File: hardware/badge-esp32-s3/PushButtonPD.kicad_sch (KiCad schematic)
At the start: 3 parts, among them SW1 TS665CJ

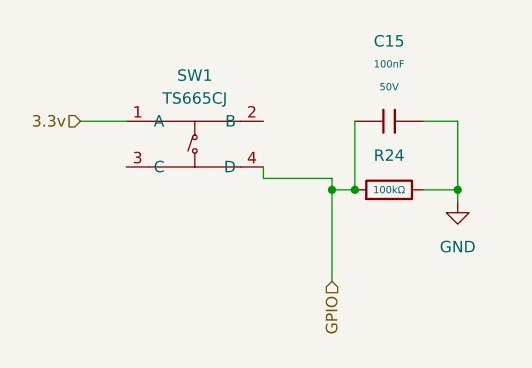
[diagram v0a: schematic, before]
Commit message: Resistor Fix
PD resistor 100k -> 47k
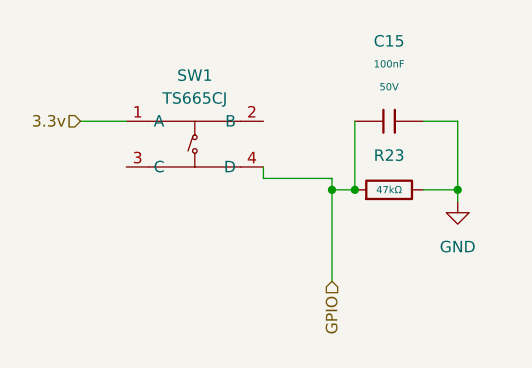
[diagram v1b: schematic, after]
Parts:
- removed R24: 100kΩ, PCM_JLCPCB:R_0805, symbol PCM_JLCPCB-Resistors:0805,100kΩ
- added R23: 47kΩ, PCM_JLCPCB:R_0805, symbol PCM_JLCPCB-Resistors:0805,47kΩ
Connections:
- net GND: now also R23.2
- net GPIO: now also R23.1

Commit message: Reapply "Merge branch 'main' into Danny"
This reverts commit 522ccfdb580e54901b8ff562dc2e90cfc327c6b7.
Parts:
- removed C15: 100nF, PCM_JLCPCB:C_0805, symbol PCM_JLCPCB-Capacitors:0805,100nF,(2)
- removed R23: 47kΩ, PCM_JLCPCB:R_0805, symbol PCM_JLCPCB-Resistors:0805,47kΩ
- added C15: 1uF, PCM_JLCPCB:C_0603, symbol PCM_JLCPCB-Capacitors:0603,1uF
- added R23, R31: 10kΩ, PCM_JLCPCB:R_0603, symbol PCM_JLCPCB-Resistors:0603,10kΩ
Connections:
- net GND: now also C15.2, R31.2
- net GPIO: now also C15.1, R23.2, R31.1; no longer SW1.4 (D)
- new net: R23.1, SW1.4 (D)

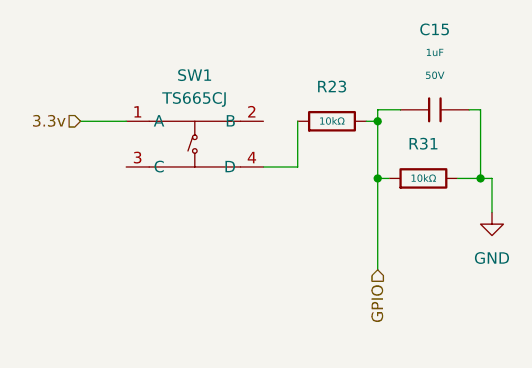
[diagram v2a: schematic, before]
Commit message: Revert "Merge branch 'main' into Danny"
This reverts commit f39a0d75d6025751b3d0be32cc251741b689ee9f, reversing
changes made to 38c8f4414de6e086c66d277d9ce522e64904a3dc.
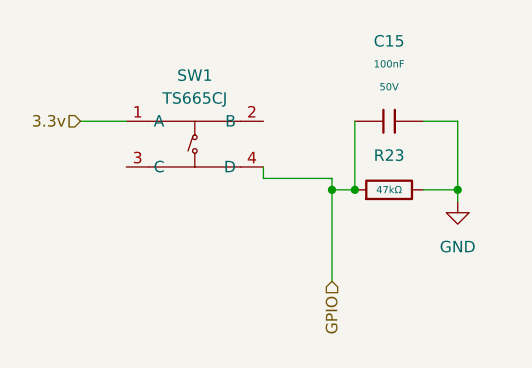
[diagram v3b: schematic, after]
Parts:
- removed C15: 1uF, PCM_JLCPCB:C_0603, symbol PCM_JLCPCB-Capacitors:0603,1uF
- removed R23, R31: 10kΩ, PCM_JLCPCB:R_0603, symbol PCM_JLCPCB-Resistors:0603,10kΩ
- added C15: 100nF, PCM_JLCPCB:C_0805, symbol PCM_JLCPCB-Capacitors:0805,100nF,(2)
- added R23: 47kΩ, PCM_JLCPCB:R_0805, symbol PCM_JLCPCB-Resistors:0805,47kΩ
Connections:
- net GND: now also C15.2, R23.2
- net GPIO: now also SW1.4 (D), C15.1, R23.1

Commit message: Updated PD schematic
Changed the button debounce schematic.
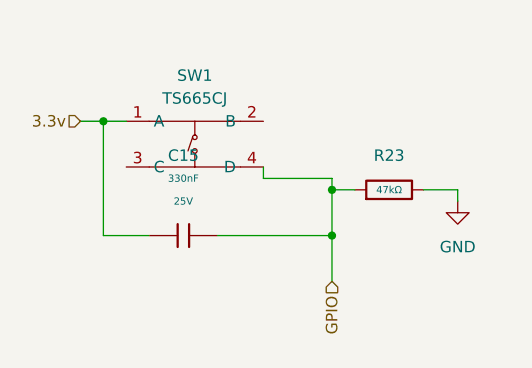
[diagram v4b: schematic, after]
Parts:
- removed C15: 100nF, PCM_JLCPCB:C_0805, symbol PCM_JLCPCB-Capacitors:0805,100nF,(2)
- added C15: 330nF, PCM_JLCPCB:C_0603, symbol PCM_JLCPCB-Capacitors:0603,330nF
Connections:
- net 3.3v: now also C15.1
- net GPIO: now also C15.2
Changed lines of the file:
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@@
 	)
 	(junction
-		(at 138.43 76.2)
+		(at 135.89 81.28)
 		(diameter 0)
 		(color 0 0 0 0)
 	)
 	(junction
-		(at 149.86 76.2)
+		(at 110.49 68.58)
 		(diameter 0)
 		(color 0 0 0 0)
@@
 	(wire
 		(pts
-			(xy 149.86 68.58) (xy 149.86 76.2)
-		)
-		(stroke
-			(width 0)
-			(type default)
-		)
-	)
-	(wire
-		(pts
 			(xy 135.89 74.93) (xy 135.89 76.2)
 		)
@@
 	(wire
 		(pts
-			(xy 146.05 68.58) (xy 149.86 68.58)
-		)
-		(stroke
-			(width 0)
-			(type default)
-		)
-	)
-	(wire
-		(pts
-			(xy 107.95 68.58) (xy 113.03 68.58)
+			(xy 107.95 68.58) (xy 110.49 68.58)
 		)
 		(stroke
@@
 	(wire
 		(pts
+			(xy 135.89 81.28) (xy 135.89 86.36)
+		)
+		(stroke
+			(width 0)
+			(type default)
+		)
+	)
+	(wire
+		(pts
 			(xy 128.27 74.93) (xy 135.89 74.93)
 		)
@@
 	(wire
 		(pts
-			(xy 135.89 76.2) (xy 135.89 86.36)
-		)
-		(stroke
-			(width 0)
-			(type default)
-		)
-	)
-	(wire
-		(pts
-			(xy 138.43 68.58) (xy 138.43 76.2)
+			(xy 135.89 76.2) (xy 135.89 81.28)
+		)
+		(stroke
+			(width 0)
+			(type default)
+		)
+	)
+	(wire
+		(pts
+			(xy 123.19 81.28) (xy 135.89 81.28)
+		)
+		(stroke
+			(width 0)
+			(type default)
+		)
+	)
+	(wire
+		(pts
+			(xy 110.49 81.28) (xy 110.49 68.58)
+		)
+		(stroke
+			(width 0)
+			(type default)
+		)
+	)
+	(wire
+		(pts
+			(xy 115.57 81.28) (xy 110.49 81.28)
 		)
 		(stroke
@@
 		(pts
 			(xy 146.05 76.2) (xy 149.86 76.2)
+		)
+		(stroke
+			(width 0)
+			(type default)
+		)
+	)
+	(wire
+		(pts
+			(xy 110.49 68.58) (xy 113.03 68.58)
 		)
 		(stroke
@@
 	)
 	(symbol
-		(lib_id "PCM_JLCPCB-Capacitors:0805,100nF,(2)")
-		(at 142.24 68.58 90)
+		(lib_id "PCM_JLCPCB-Capacitors:0603,330nF")
+		(at 119.38 81.28 90)
 		(unit 1)
 		(exclude_from_sim no)
@@
 		(fields_autoplaced yes)
 		(property "Reference" "C15"
-			(at 142.24 59.69 90)
-			(effects
-				(font
-					(size 1.27 1.27)
-				)
-			)
-		)
-		(property "Value" "100nF"
-			(at 142.24 62.23 90)
+			(at 119.38 72.39 90)
+			(effects
+				(font
+					(size 1.27 1.27)
+				)
+			)
+		)
+		(property "Value" "330nF"
+			(at 119.38 74.93 90)
 			(effects
 				(font
@@
 			)
 		)
-		(property "Footprint" "PCM_JLCPCB:C_0805"
-			(at 142.24 70.358 90)
-			(effects
-				(font
-					(size 1.27 1.27)
-				)
-				(hide yes)
-			)
-		)
-		(property "Datasheet" "https://www.lcsc.com/datasheet/lcsc_datasheet_2304140030_YAGEO-CC0805KRX7R9BB104_C49678.pdf"
-			(at 142.24 68.58 0)
-			(effects
-				(font
-					(size 1.27 1.27)
-				)
-				(hide yes)
-			)
-		)
-		(property "Description" "50V 100nF X7R ±10% 0805 Multilayer Ceramic Capacitors MLCC - SMD/SMT ROHS"
-			(at 142.24 68.58 0)
-			(effects
-				(font
-					(size 1.27 1.27)
-				)
-				(hide yes)
-			)
-		)
-		(property "LCSC" "C49678"
-			(at 142.24 68.58 0)
-			(effects
-				(font
-					(size 1.27 1.27)
-				)
-				(hide yes)
-			)
-		)
-		(property "Stock" "23739199"
-			(at 142.24 68.58 0)
-			(effects
-				(font
-					(size 1.27 1.27)
-				)
-				(hide yes)
-			)
-		)
-		(property "Price" "0.008USD"
-			(at 142.24 68.58 0)
+		(property "Footprint" "PCM_JLCPCB:C_0603"
+			(at 119.38 83.058 90)
+			(effects
+				(font
+					(size 1.27 1.27)
+				)
+				(hide yes)
+			)
+		)
+		(property "Datasheet" "https://www.lcsc.com/datasheet/lcsc_datasheet_2304140030_FH--Guangdong-Fenghua-Advanced-Tech-0603B334K250NT_C1615.pdf"
+			(at 119.38 81.28 0)
+			(effects
+				(font
+					(size 1.27 1.27)
+				)
+				(hide yes)
+			)
+		)
+		(property "Description" "25V 330nF X7R ±10% 0603 Multilayer Ceramic Capacitors MLCC - SMD/SMT ROHS"
+			(at 119.38 81.28 0)
+			(effects
+				(font
+					(size 1.27 1.27)
+				)
+				(hide yes)
+			)
+		)
+		(property "LCSC" "C1615"
+			(at 119.38 81.28 0)
+			(effects
+				(font
+					(size 1.27 1.27)
+				)
+				(hide yes)
+			)
+		)
+		(property "Stock" "122277"
+			(at 119.38 81.28 0)
+			(effects
+				(font
+					(size 1.27 1.27)
+				)
+				(hide yes)
+			)
+		)
+		(property "Price" "0.014USD"
+			(at 119.38 81.28 0)
 			(effects
 				(font
@@
 		)
 		(property "Process" "SMT"
-			(at 142.24 68.58 0)
+			(at 119.38 81.28 0)
 			(effects
 				(font
@@
 		)
 		(property "Minimum Qty" "20"
-			(at 142.24 68.58 0)
+			(at 119.38 81.28 0)
 			(effects
 				(font
@@
 		)
 		(property "Attrition Qty" "10"
-			(at 142.24 68.58 0)
-			(effects
-				(font
-					(size 1.27 1.27)
-				)
-				(hide yes)
-			)
-		)
-		(property "Class" "Basic Component"
-			(at 142.24 68.58 0)
+			(at 119.38 81.28 0)
+			(effects
+				(font
+					(size 1.27 1.27)
+				)
+				(hide yes)
+			)
+		)
+		(property "Class" "Preferred Component"
+			(at 119.38 81.28 0)
 			(effects
 				(font
@@
 		)
 		(property "Category" "Capacitors,Multilayer Ceramic Capacitors MLCC - SMD/SMT"
-			(at 142.24 68.58 0)
-			(effects
-				(font
-					(size 1.27 1.27)
-				)
-				(hide yes)
-			)
-		)
-		(property "Manufacturer" "YAGEO"
-			(at 142.24 68.58 0)
-			(effects
-				(font
-					(size 1.27 1.27)
-				)
-				(hide yes)
-			)
-		)
-		(property "Part" "CC0805KRX7R9BB104"
-			(at 142.24 68.58 0)
-			(effects
-				(font
-					(size 1.27 1.27)
-				)
-				(hide yes)
-			)
-		)
-		(property "Voltage Rated" "50V"
-			(at 142.24 64.77 90)
+			(at 119.38 81.28 0)
+			(effects
+				(font
+					(size 1.27 1.27)
+				)
+				(hide yes)
+			)
+		)
+		(property "Manufacturer" "FH(Guangdong Fenghua Advanced Tech)"
+			(at 119.38 81.28 0)
+			(effects
+				(font
+					(size 1.27 1.27)
+				)
+				(hide yes)
+			)
+		)
+		(property "Part" "0603B334K250NT"
+			(at 119.38 81.28 0)
+			(effects
+				(font
+					(size 1.27 1.27)
+				)
+				(hide yes)
+			)
+		)
+		(property "Voltage Rated" "25V"
+			(at 119.38 77.47 90)
 			(effects
 				(font
@@
 		)
 		(property "Tolerance" "±10%"
-			(at 142.24 68.58 0)
-			(effects
-				(font
-					(size 1.27 1.27)
-				)
-				(hide yes)
-			)
-		)
-		(property "Capacitance" "100nF"
-			(at 142.24 68.58 0)
+			(at 119.38 81.28 0)
+			(effects
+				(font
+					(size 1.27 1.27)
+				)
+				(hide yes)
+			)
+		)
+		(property "Capacitance" "330nF"
+			(at 119.38 81.28 0)
 			(effects
 				(font
@@
 		)
 		(property "Temperature Coefficient" "X7R"
-			(at 142.24 68.58 0)
+			(at 119.38 81.28 0)
 			(effects
 				(font
@@
 		)
 		(instances
-			(project "badge-esp32-s3"
+			(project ""
 				(path "/e2af9a6c-dbe9-4de2-9ba6-ea213a7300ec/9feb22ac-0492-47b5-89fe-3e77a54de168/0c6f020c-1e0e-43cd-8a36-0a56f6d3220b"
 					(reference "C17")
@@
 				)
 				(path "/e2af9a6c-dbe9-4de2-9ba6-ea213a7300ec/9feb22ac-0492-47b5-89fe-3e77a54de168/26f14f73-3c64-431d-bfa5-e30d3515d6c4"
-					(reference "C?")
-					(unit 1)
-				)
+					(reference "C23")
+					(unit 1)
+				)

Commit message: PD updated once again
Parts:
- removed C15: 330nF, PCM_JLCPCB:C_0603, symbol PCM_JLCPCB-Capacitors:0603,330nF
- removed R23: 47kΩ, PCM_JLCPCB:R_0805, symbol PCM_JLCPCB-Resistors:0805,47kΩ
- added C15: 1uF, PCM_JLCPCB:C_0603, symbol PCM_JLCPCB-Capacitors:0603,1uF
- added R23, R31: 10kΩ, PCM_JLCPCB:R_0603, symbol PCM_JLCPCB-Resistors:0603,10kΩ
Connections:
- net GND: now also C15.2, R31.2
- net GPIO: now also C15.1, R23.2, R31.1; no longer SW1.4 (D)
- new net: R23.1, SW1.4 (D)

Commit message: Annotate schematic
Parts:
- renumbered C15 to C18, R23 to R27, R31 to R28, SW1 to SW4
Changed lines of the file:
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@@
 		(dnp no)
 		(fields_autoplaced yes)
-		(property "Reference" "SW1"
+		(property "Reference" "SW4"
 			(at 120.65 63.5 0)
 			(effects
@@
 			(project "badge-esp32-s3"
 				(path "/e2af9a6c-dbe9-4de2-9ba6-ea213a7300ec/9feb22ac-0492-47b5-89fe-3e77a54de168/0c6f020c-1e0e-43cd-8a36-0a56f6d3220b"
+					(reference "SW6")
+					(unit 1)
+				)
+				(path "/e2af9a6c-dbe9-4de2-9ba6-ea213a7300ec/9feb22ac-0492-47b5-89fe-3e77a54de168/26f14f73-3c64-431d-bfa5-e30d3515d6c4"
+					(reference "SW9")
+					(unit 1)
+				)
+				(path "/e2af9a6c-dbe9-4de2-9ba6-ea213a7300ec/9feb22ac-0492-47b5-89fe-3e77a54de168/a24e4638-e764-42f8-9a03-a3574c3b6e5b"
 					(reference "SW4")
 					(unit 1)
 				)
-				(path "/e2af9a6c-dbe9-4de2-9ba6-ea213a7300ec/9feb22ac-0492-47b5-89fe-3e77a54de168/26f14f73-3c64-431d-bfa5-e30d3515d6c4"
+				(path "/e2af9a6c-dbe9-4de2-9ba6-ea213a7300ec/9feb22ac-0492-47b5-89fe-3e77a54de168/b99b1c65-2141-4657-af08-7b837c45a510"
+					(reference "SW5")
+					(unit 1)
+				)
+				(path "/e2af9a6c-dbe9-4de2-9ba6-ea213a7300ec/9feb22ac-0492-47b5-89fe-3e77a54de168/f11ff8f0-58bf-4f8c-9221-02eb2354874a"
+					(reference "SW7")
+					(unit 1)
+				)
+				(path "/e2af9a6c-dbe9-4de2-9ba6-ea213a7300ec/9feb22ac-0492-47b5-89fe-3e77a54de168/fb6d2a04-654d-4115-8ed9-b9891bab072c"
 					(reference "SW8")
-					(unit 1)
-				)
-				(path "/e2af9a6c-dbe9-4de2-9ba6-ea213a7300ec/9feb22ac-0492-47b5-89fe-3e77a54de168/a24e4638-e764-42f8-9a03-a3574c3b6e5b"
-					(reference "SW1")
-					(unit 1)
-				)
-				(path "/e2af9a6c-dbe9-4de2-9ba6-ea213a7300ec/9feb22ac-0492-47b5-89fe-3e77a54de168/b99b1c65-2141-4657-af08-7b837c45a510"
-					(reference "SW3")
-					(unit 1)
-				)
-				(path "/e2af9a6c-dbe9-4de2-9ba6-ea213a7300ec/9feb22ac-0492-47b5-89fe-3e77a54de168/f11ff8f0-58bf-4f8c-9221-02eb2354874a"
-					(reference "SW5")
-					(unit 1)
-				)
-				(path "/e2af9a6c-dbe9-4de2-9ba6-ea213a7300ec/9feb22ac-0492-47b5-89fe-3e77a54de168/fb6d2a04-654d-4115-8ed9-b9891bab072c"
-					(reference "SW6")
 					(unit 1)
 				)
@@
 		(dnp no)
 		(fields_autoplaced yes)
-		(property "Reference" "#PWR038"
+		(property "Reference" "#PWR052"
 			(at 153.67 85.09 0)
 			(effects
@@
 			(project "badge-esp32-s3"
 				(path "/e2af9a6c-dbe9-4de2-9ba6-ea213a7300ec/9feb22ac-0492-47b5-89fe-3e77a54de168/0c6f020c-1e0e-43cd-8a36-0a56f6d3220b"
-					(reference "#PWR040")
+					(reference "#PWR054")
 					(unit 1)
 				)
 				(path "/e2af9a6c-dbe9-4de2-9ba6-ea213a7300ec/9feb22ac-0492-47b5-89fe-3e77a54de168/26f14f73-3c64-431d-bfa5-e30d3515d6c4"
-					(reference "#PWR042")
+					(reference "#PWR058")
 					(unit 1)
 				)
 				(path "/e2af9a6c-dbe9-4de2-9ba6-ea213a7300ec/9feb22ac-0492-47b5-89fe-3e77a54de168/a24e4638-e764-42f8-9a03-a3574c3b6e5b"
-					(reference "#PWR038")
+					(reference "#PWR052")
 					(unit 1)
 				)
 				(path "/e2af9a6c-dbe9-4de2-9ba6-ea213a7300ec/9feb22ac-0492-47b5-89fe-3e77a54de168/b99b1c65-2141-4657-af08-7b837c45a510"
-					(reference "#PWR039")
+					(reference "#PWR053")
 					(unit 1)
 				)
 				(path "/e2af9a6c-dbe9-4de2-9ba6-ea213a7300ec/9feb22ac-0492-47b5-89fe-3e77a54de168/f11ff8f0-58bf-4f8c-9221-02eb2354874a"
-					(reference "#PWR041")
+					(reference "#PWR055")
 					(unit 1)
 				)
 				(path "/e2af9a6c-dbe9-4de2-9ba6-ea213a7300ec/9feb22ac-0492-47b5-89fe-3e77a54de168/fb6d2a04-654d-4115-8ed9-b9891bab072c"
-					(reference "#PWR043")
+					(reference "#PWR056")
 					(unit 1)
 				)
@@
 		(dnp no)
 		(fields_autoplaced yes)
-		(property "Reference" "C15"
+		(property "Reference" "C18"
 			(at 147.32 58.42 90)
 			(effects
@@
 			(project ""
 				(path "/e2af9a6c-dbe9-4de2-9ba6-ea213a7300ec/9feb22ac-0492-47b5-89fe-3e77a54de168/0c6f020c-1e0e-43cd-8a36-0a56f6d3220b"
-					(reference "C17")
+					(reference "C20")
 					(unit 1)
 				)
@@
 				)
 				(path "/e2af9a6c-dbe9-4de2-9ba6-ea213a7300ec/9feb22ac-0492-47b5-89fe-3e77a54de168/a24e4638-e764-42f8-9a03-a3574c3b6e5b"
-					(reference "C15")
+					(reference "C18")
 					(unit 1)
 				)
 				(path "/e2af9a6c-dbe9-4de2-9ba6-ea213a7300ec/9feb22ac-0492-47b5-89fe-3e77a54de168/b99b1c65-2141-4657-af08-7b837c45a510"
-					(reference "C16")
+					(reference "C19")
 					(unit 1)
 				)
 				(path "/e2af9a6c-dbe9-4de2-9ba6-ea213a7300ec/9feb22ac-0492-47b5-89fe-3e77a54de168/f11ff8f0-58bf-4f8c-9221-02eb2354874a"
-					(reference "C18")
+					(reference "C21")
 					(unit 1)
 				)
 				(path "/e2af9a6c-dbe9-4de2-9ba6-ea213a7300ec/9feb22ac-0492-47b5-89fe-3e77a54de168/fb6d2a04-654d-4115-8ed9-b9891bab072c"
-					(reference "C19")
+					(reference "C22")
 					(unit 1)
 				)
@@
 		(dnp no)
 		(fields_autoplaced yes)
-		(property "Reference" "R31"
+		(property "Reference" "R28"
 			(at 146.05 71.12 90)
 			(effects
@@
 			(project "badge-esp32-s3"
 				(path "/e2af9a6c-dbe9-4de2-9ba6-ea213a7300ec/9feb22ac-0492-47b5-89fe-3e77a54de168/0c6f020c-1e0e-43cd-8a36-0a56f6d3220b"
-					(reference "R33")
+					(reference "R32")
 					(unit 1)
 				)
 				(path "/e2af9a6c-dbe9-4de2-9ba6-ea213a7300ec/9feb22ac-0492-47b5-89fe-3e77a54de168/26f14f73-3c64-431d-bfa5-e30d3515d6c4"
-					(reference "R36")
+					(reference "R38")
 					(unit 1)
 				)
 				(path "/e2af9a6c-dbe9-4de2-9ba6-ea213a7300ec/9feb22ac-0492-47b5-89fe-3e77a54de168/a24e4638-e764-42f8-9a03-a3574c3b6e5b"
-					(reference "R31")
+					(reference "R28")
 					(unit 1)
 				)
 				(path "/e2af9a6c-dbe9-4de2-9ba6-ea213a7300ec/9feb22ac-0492-47b5-89fe-3e77a54de168/b99b1c65-2141-4657-af08-7b837c45a510"
-					(reference "R32")
+					(reference "R30")
 					(unit 1)
 				)
@@
 				)
 				(path "/e2af9a6c-dbe9-4de2-9ba6-ea213a7300ec/9feb22ac-0492-47b5-89fe-3e77a54de168/fb6d2a04-654d-4115-8ed9-b9891bab072c"
-					(reference "R35")
+					(reference "R36")
 					(unit 1)
 				)
@@
 		(dnp no)
 		(fields_autoplaced yes)
-		(property "Reference" "R23"
+		(property "Reference" "R27"
 			(at 135.89 64.77 90)
 			(effects
@@
 			(project ""
 				(path "/e2af9a6c-dbe9-4de2-9ba6-ea213a7300ec/9feb22ac-0492-47b5-89fe-3e77a54de168/0c6f020c-1e0e-43cd-8a36-0a56f6d3220b"
-					(reference "R25")
+					(reference "R31")
 					(unit 1)
 				)
 				(path "/e2af9a6c-dbe9-4de2-9ba6-ea213a7300ec/9feb22ac-0492-47b5-89fe-3e77a54de168/26f14f73-3c64-431d-bfa5-e30d3515d6c4"
-					(reference "R28")
+					(reference "R37")
 					(unit 1)
 				)
 				(path "/e2af9a6c-dbe9-4de2-9ba6-ea213a7300ec/9feb22ac-0492-47b5-89fe-3e77a54de168/a24e4638-e764-42f8-9a03-a3574c3b6e5b"
-					(reference "R23")
+					(reference "R27")
 					(unit 1)
 				)
 				(path "/e2af9a6c-dbe9-4de2-9ba6-ea213a7300ec/9feb22ac-0492-47b5-89fe-3e77a54de168/b99b1c65-2141-4657-af08-7b837c45a510"
-					(reference "R24")
+					(reference "R29")
 					(unit 1)
 				)
 				(path "/e2af9a6c-dbe9-4de2-9ba6-ea213a7300ec/9feb22ac-0492-47b5-89fe-3e77a54de168/f11ff8f0-58bf-4f8c-9221-02eb2354874a"
-					(reference "R26")
+					(reference "R33")
 					(unit 1)
 				)
 				(path "/e2af9a6c-dbe9-4de2-9ba6-ea213a7300ec/9feb22ac-0492-47b5-89fe-3e77a54de168/fb6d2a04-654d-4115-8ed9-b9891bab072c"
-					(reference "R27")
-					(unit 1)
-				)
+					(reference "R35")
+					(unit 1)
+				)

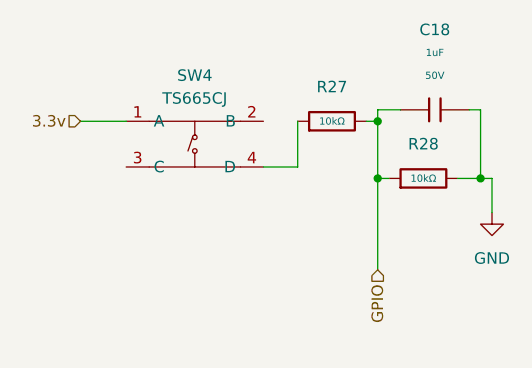
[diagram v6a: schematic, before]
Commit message: Fix some DRC errors
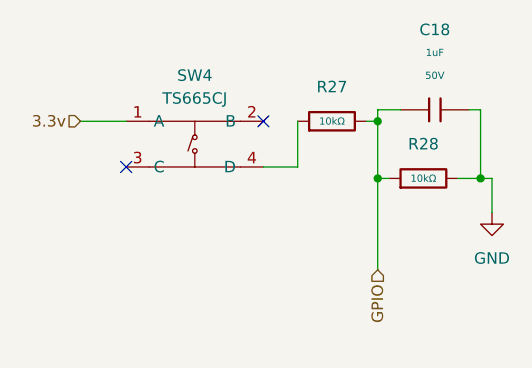
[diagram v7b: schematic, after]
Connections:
- no-connect marks 0 -> 2
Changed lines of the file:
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@@
 		(color 0 0 0 0)
+	)
+	(no_connect
+		(at 128.27 68.58)
+	)
+	(no_connect
+		(at 113.03 73.66)
 	)
 	(wire

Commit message: Update PushButtonPD.kicad_sch
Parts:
- renumbered C18 to C?, R28 to R?, R27 to R?, SW4 to SW?
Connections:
- net GND: now also R?.2; no longer R?.2
- net GPIO: now also R?.2; no longer R?.1, R?.2
- net at R?.1, SW?.4 (D): now also R?.1
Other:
- moved on the sheet: C?, R?, SW?
